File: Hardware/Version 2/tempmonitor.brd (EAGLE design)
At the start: 100 x 50 mm, 33 parts, among them IC1 74LS595D, IC2 74LS595D, IC3 74LS595D, IC4 74LS595D, IC5 74LS595D, J2 TP_8, J3 USB-MICROB, T1 NPN, T2 NPN, T3 NPN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

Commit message: Added loggos
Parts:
- added LOGO1: OSHW-LOGOL, SparkFun-Aesthetics:OSHW-LOGO-L
- added U$1, U$2: LOGO, TempMonitor:LOGO_M
- added U$3: ROHS_LOGO, SparkFun-Aesthetics:ROHS_LOGO_0.18_IN
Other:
- board text added: "2016 Verison 1.0"
- board text added: "tempmonitor.se"
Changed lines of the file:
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@@
 <setting verticaltext="up"/>
 </settings>
-<grid distance="0.001" unitdist="inch" unit="inch" style="lines" multiple="1" display="yes" altdistance="0.025" altunitdist="inch" altunit="inch"/>
+<grid distance="1" unitdist="mm" unit="mm" style="lines" multiple="1" display="yes" altdistance="0.025" altunitdist="inch" altunit="inch"/>
 <layers>
 <layer number="1" name="Top" color="4" fill="1" visible="yes" active="yes"/>
@@
 <wire x1="100" y1="50" x2="100" y2="0" width="0" layer="20"/>
 <wire x1="0" y1="50" x2="0" y2="0" width="0" layer="20"/>
+<text x="73.3044" y="3.2766" size="1.778" layer="22" rot="MR180">2016 Verison 1.0</text>
+<text x="44.45" y="3.0226" size="1.778" layer="22" rot="MR180">tempmonitor.se</text>
 </plain>
 <attributes>
@@
 <attribute name="NAME" x="11.8108" y="3.4854" size="1.016" layer="26" rot="MR0"/>
 </element>
+<element name="U$1" library="TempMonitor" package="LOGO_M" value="LOGO" x="2.1844" y="41.0464" rot="R270"/>
+<element name="U$2" library="TempMonitor" package="LOGO_M" value="LOGO" x="91.5416" y="3.937" rot="MR0"/>
+<element name="LOGO1" library="SparkFun-Aesthetics" package="OSHW-LOGO-L" value="OSHW-LOGOL" x="53.4162" y="6.5024" rot="MR0"/>
+<element name="U$3" library="SparkFun-Aesthetics" package="ROHS_LOGO_0.18_IN" value="ROHS_LOGO" x="48.2346" y="4.2926" rot="MR0"/>
 </elements>
 <signals>

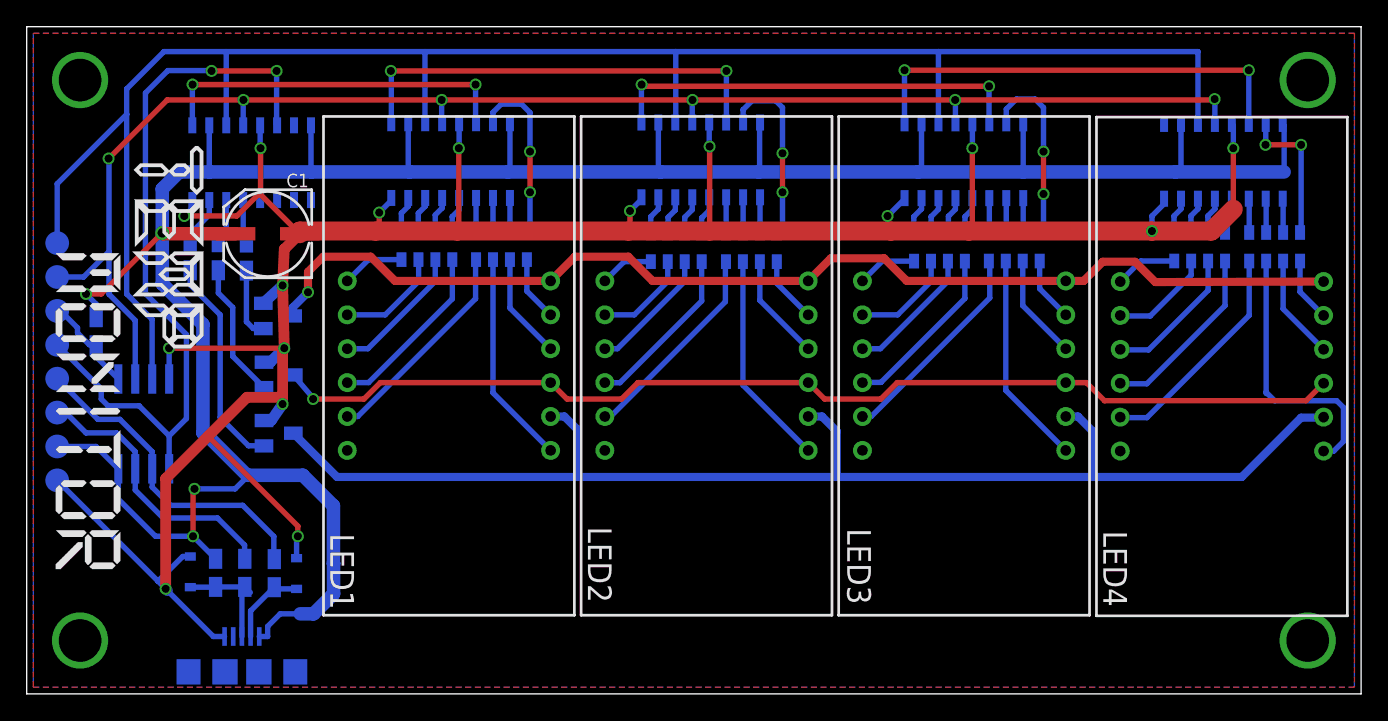
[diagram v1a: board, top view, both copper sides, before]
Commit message: USB circuit fix
USB circuit fix R3 incorrectly connected. Added filtering capacitors to MCU and shift registers. Centered displays.
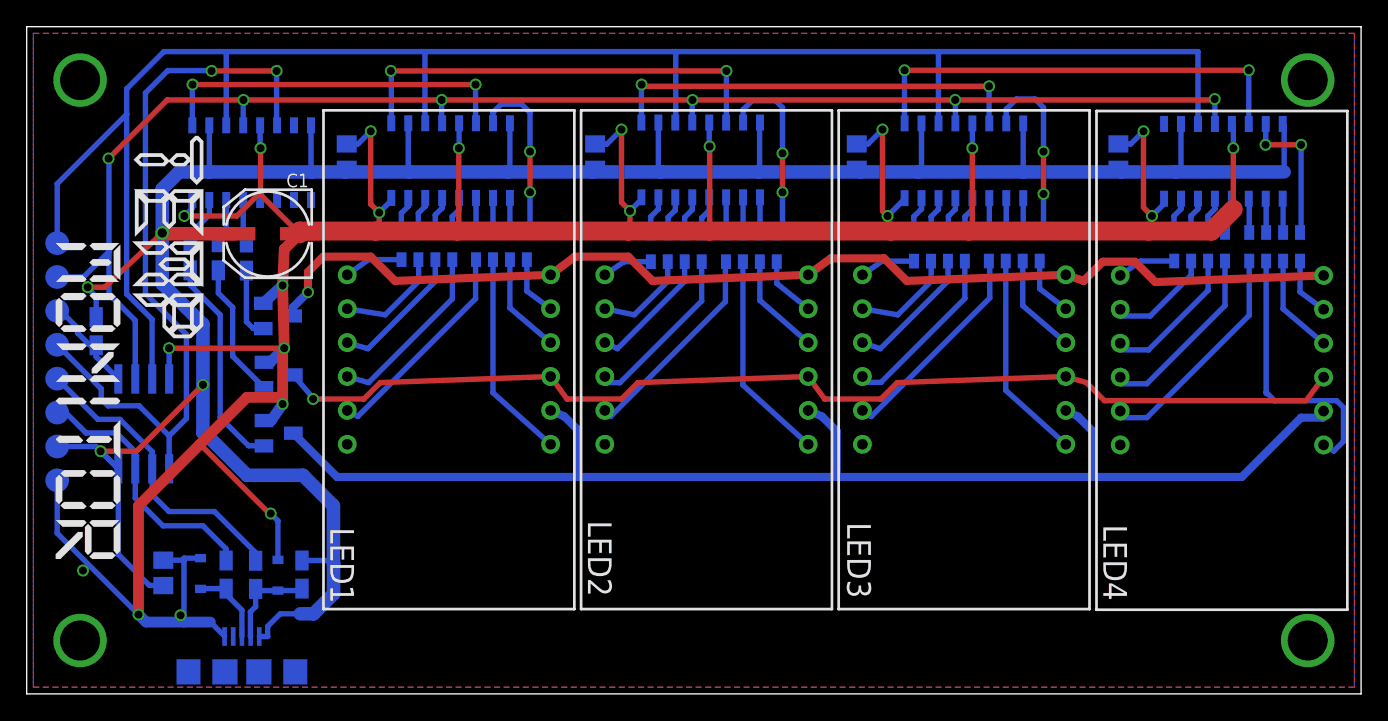
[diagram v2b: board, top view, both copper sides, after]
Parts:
- removed U$3: ROHS_LOGO, SparkFun-Aesthetics:ROHS_LOGO_0.18_IN
- added C2, C3, C4, C5, C6: 0.1uF, resistor:C0805
- moved R3 6.48 mm to (20.6, 8.94)
- moved D1 1.40 mm to (18.8, 8.89)
- moved R1 1.40 mm to (17.2, 8.92)
- moved R2 1.40 mm to (14.9, 8.94)
- moved D2 0.77 mm to (13.0, 9.02)
- moved U$1 0.76 mm to (2.18, 41.8)
- moved LOGO1 0.65 mm to (54.1, 6.38)
- moved LED1 0.46 mm to (31.6, 25.1)
- moved LED2 0.46 mm to (50.9, 25.1)
- moved LED3 0.46 mm to (70.3, 25.1)
- moved LED4 0.46 mm to (89.6, 25.0)
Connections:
- net +5V: now also C2.1, C3.1, C4.1, C5.1, C6.2
- net GND: now also C2.2, C3.2, C4.2, C5.2, C6.1
- net N$1: now also R3.1
- net N$2: no longer R3.1
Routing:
- net GND: track 213.1 -> 257.1 mm, vias 16 -> 22
- net +5V: track 207.0 -> 214.8 mm
- net N$2: track 8.87 -> 6.24 mm
- net D-: track 24.7 -> 23.1 mm
- net N$1: track 6.17 -> 7.34 mm
- net GND_D2: track 81.7 -> 82.9 mm
- net D+: track 20.9 -> 19.8 mm
- net GND_D3: track 98.5 -> 99.2 mm

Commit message: Fix LED display wiring
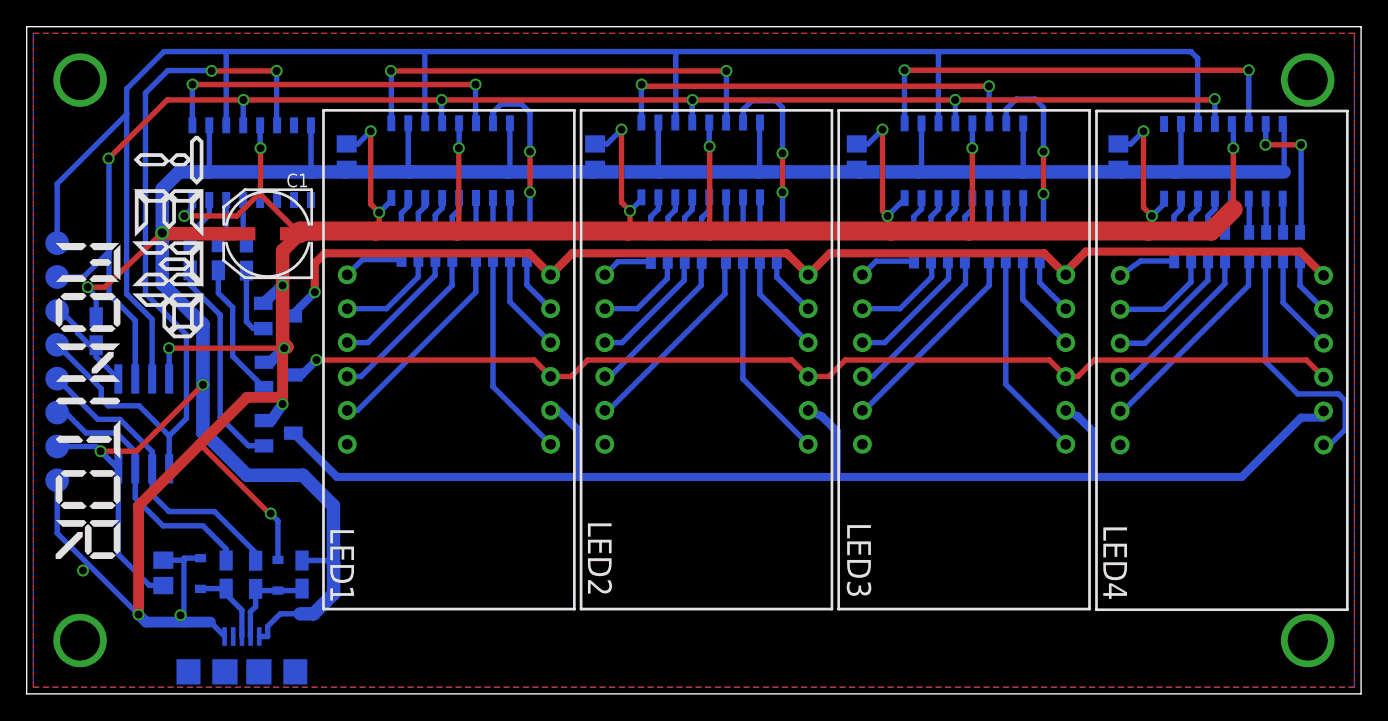
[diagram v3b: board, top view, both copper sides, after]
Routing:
- net N$72: track 17.4 -> 15.4 mm
- net N$69: track 20.7 -> 19.0 mm
- net N$68: track 14.1 -> 12.5 mm
- net GND_D2: track 82.9 -> 81.3 mm
- net N$31: track 13.2 -> 11.8 mm
- net N$53: track 13.5 -> 12.3 mm
- net N$73: track 11.1 -> 9.98 mm
- net N$57: track 16.2 -> 15.2 mm
- net N$13: track 13.5 -> 12.6 mm
- net GND_D1: track 84.8 -> 85.5 mm
- net N$41: track 15.8 -> 15.1 mm
- net N$17: track 16.3 -> 15.8 mm
- net N$19: track 10.4 -> 9.86 mm

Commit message: PCB fix
Removed C6 value+ more space for R3, R1 & D1
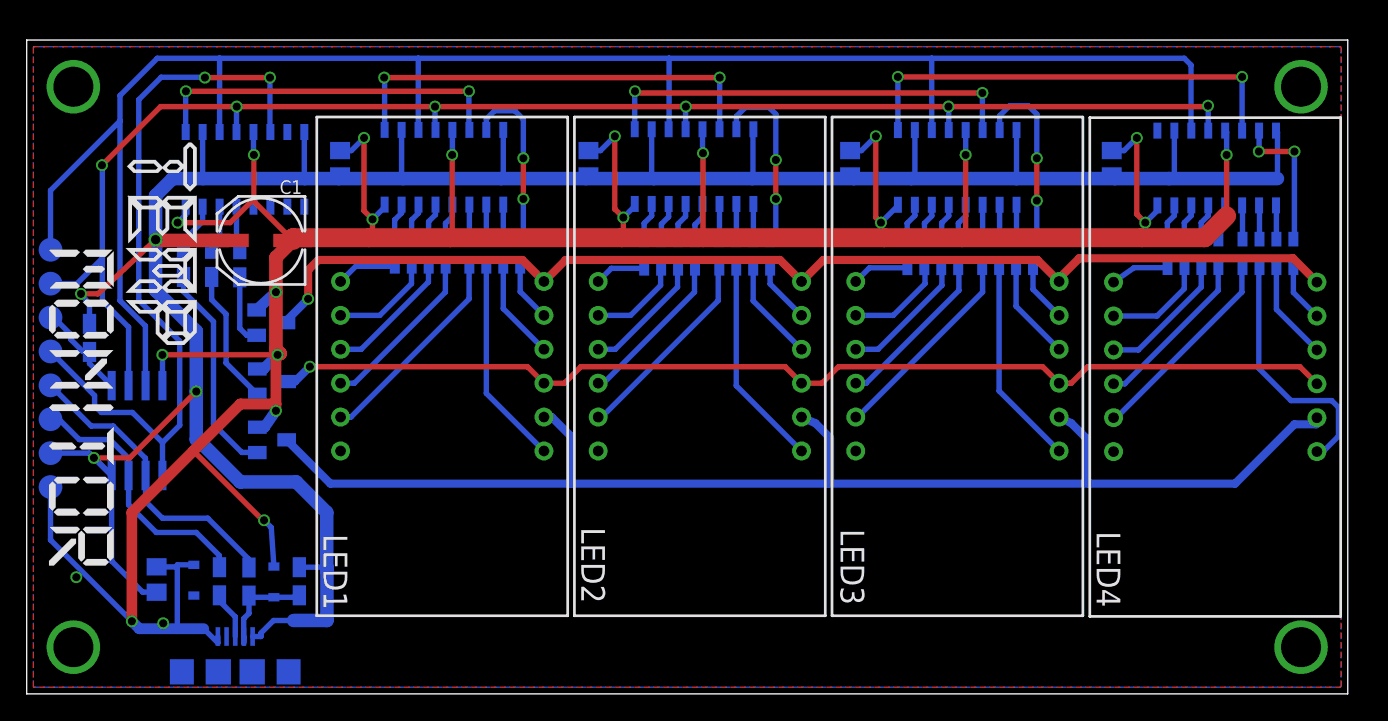
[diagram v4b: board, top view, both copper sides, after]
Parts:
- moved U$1 0.71 mm to (1.68, 41.3)
- moved C1 0.71 mm to (17.6, 34.0)
- moved C2 0.71 mm to (81.3, 39.8)
- moved C3 0.71 mm to (61.7, 39.8)
- moved C4 0.71 mm to (42.1, 39.8)
- moved C5 0.71 mm to (23.5, 39.8)
- moved C6 0.71 mm to (9.74, 8.57)
- moved D2 0.71 mm to (12.5, 8.52)
- moved IC1 0.71 mm to (50.0, 39.5)
- moved IC2 0.71 mm to (31.3, 39.5)
- moved IC3 0.71 mm to (69.7, 39.5)
- moved IC4 0.71 mm to (16.4, 39.3)
- moved IC5 0.71 mm to (89.2, 39.4)
- moved LED1 0.71 mm to (31.1, 24.6)
- moved LED2 0.71 mm to (50.4, 24.6)
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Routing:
- net N$2: track 6.24 -> 3.84 mm
- net N$1: track 7.34 -> 8.07 mm
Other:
- board size 100 x 50 mm -> 99 x 49 mm
